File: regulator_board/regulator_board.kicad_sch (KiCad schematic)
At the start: 68 parts, among them J1 BATT, J10 5VOUT, J11 9VOUT, J12 9VOUT, J13 9VOUT, J2 5VOUT, J3 5VOUT, J4 5VOUT, J5 5VOUT, J6 5VOUT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

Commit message: regulator board title block
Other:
- company: (none) -> AUVCalStateLA
- title: (none) -> Regulator Board
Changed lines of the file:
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@@
 (kicad_sch (version 20211123) (generator eeschema)
   (paper "A4")
+  (title_block
+    (title "Regulator Board")
+    (date "2023-01-11")
+    (rev "dev1")
+    (company "AUVCalStateLA")
+  )
   (junction (at 160.02 86.36) (diameter 0) (color 0 0 0 0)
   )

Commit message: regulator component footprints
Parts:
- J1: footprint (none) -> Connector_AMASS:AMASS_XT60-M_1x02_P7.20mm_Vertical
- JP1, JP2, JP3, JP4: footprint (none) -> Jumper:SolderJumper-2_P1.3mm_Bridged_RoundedPad1.0x1.5mm
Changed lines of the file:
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@@
     (property "Reference" "JP3" (id 0) (at 166.37 80.01 0))
     (property "Value" "EN" (id 1) (at 166.37 82.55 0))
-    (property "Footprint" "" (id 2) (at 166.37 86.36 0)
+    (property "Footprint" "Jumper:SolderJumper-2_P1.3mm_Bridged_RoundedPad1.0x1.5mm" (id 2) (at 166.37 86.36 0)
       (effects (font (size 1.27 1.27)) hide)
     )
@@
     (property "Reference" "JP1" (id 0) (at 39.37 80.01 0))
     (property "Value" "EN" (id 1) (at 39.37 82.55 0))
-    (property "Footprint" "" (id 2) (at 39.37 86.36 0)
+    (property "Footprint" "Jumper:SolderJumper-2_P1.3mm_Bridged_RoundedPad1.0x1.5mm" (id 2) (at 39.37 86.36 0)
       (effects (font (size 1.27 1.27)) hide)
     )
@@
     (property "Reference" "JP4" (id 0) (at 166.37 130.81 0))
     (property "Value" "EN" (id 1) (at 166.37 133.35 0))
-    (property "Footprint" "" (id 2) (at 166.37 137.16 0)
+    (property "Footprint" "Jumper:SolderJumper-2_P1.3mm_Bridged_RoundedPad1.0x1.5mm" (id 2) (at 166.37 137.16 0)
       (effects (font (size 1.27 1.27)) hide)
     )
@@
     (property "Reference" "JP2" (id 0) (at 39.37 130.81 0))
     (property "Value" "EN" (id 1) (at 39.37 133.35 0))
-    (property "Footprint" "" (id 2) (at 39.37 137.16 0)
+    (property "Footprint" "Jumper:SolderJumper-2_P1.3mm_Bridged_RoundedPad1.0x1.5mm" (id 2) (at 39.37 137.16 0)
       (effects (font (size 1.27 1.27)) hide)
     )
@@
     (property "Reference" "J1" (id 0) (at 36.83 34.29 0))
     (property "Value" "BATT" (id 1) (at 36.83 36.83 0))
-    (property "Footprint" "" (id 2) (at 36.83 40.64 0)
+    (property "Footprint" "Connector_AMASS:AMASS_XT60-M_1x02_P7.20mm_Vertical" (id 2) (at 36.83 40.64 0)
       (effects (font (size 1.27 1.27)) hide)
     )
@@
     )
     (path "/b2e2fd19-798d-493c-9b57-86fa6fbcae53"
-      (reference "J1") (unit 1) (value "BATT") (footprint "")
+      (reference "J1") (unit 1) (value "BATT") (footprint "Connector_AMASS:AMASS_XT60-M_1x02_P7.20mm_Vertical")
     )
     (path "/580b5f68-7f84-4073-8ca8-221bc33e2978"
@@
     )
     (path "/2bf21a6a-e878-46f9-9e74-f711cf10453a"
-      (reference "JP1") (unit 1) (value "EN") (footprint "")
+      (reference "JP1") (unit 1) (value "EN") (footprint "Jumper:SolderJumper-2_P1.3mm_Bridged_RoundedPad1.0x1.5mm")
     )
     (path "/5a3ed22b-6215-4f1c-ae8e-2997d5637ba2"
-      (reference "JP2") (unit 1) (value "EN") (footprint "")
+      (reference "JP2") (unit 1) (value "EN") (footprint "Jumper:SolderJumper-2_P1.3mm_Bridged_RoundedPad1.0x1.5mm")
     )
     (path "/1ec1446c-1ce8-40a1-b2a2-29f00b72424b"
-      (reference "JP3") (unit 1) (value "EN") (footprint "")
+      (reference "JP3") (unit 1) (value "EN") (footprint "Jumper:SolderJumper-2_P1.3mm_Bridged_RoundedPad1.0x1.5mm")
     )
     (path "/4de0ee0c-c3e9-4dca-8da2-aaf3a6650e2e"
-      (reference "JP4") (unit 1) (value "EN") (footprint "")
+      (reference "JP4") (unit 1) (value "EN") (footprint "Jumper:SolderJumper-2_P1.3mm_Bridged_RoundedPad1.0x1.5mm")
     )
     (path "/318d6667-d175-4fcf-834c-669cc0534e5a"

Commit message: regulator board prelimiary completion
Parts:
- C1, C10, C11, C12, C13, C14, C15, C16, C17, C18, C19, C2, C20, C3, C4, C5, C6, C7, C8, C9: footprint (none) -> Capacitor_SMD:C_0603_1608Metric_Pad1.08x0.95mm_HandSolder
- D1, D2, D3, D4, D5: footprint (none) -> LED_SMD:LED_0603_1608Metric_Pad1.05x0.95mm_HandSolder
- F1: footprint (none) -> Fuse:Fuseholder_Blade_Mini_Keystone_3568
- F2, F3, F4, F5: footprint (none) -> Fuse:Fuse_0603_1608Metric_Pad1.05x0.95mm_HandSolder
- J10, J11, J12, J13, J2, J3, J4, J5, J6, J7, J8, J9: footprint (none) -> Connector_JST:JST_XH_B2B-XH-A_1x02_P2.50mm_Vertical
- L1, L2, L3, L4: footprint (none) -> AUVCSLA_FootLib:L_Bourns_SRP6030
- R1, R10, R11, R12, R13, R2, R3, R4, R5, R6, R7, R8, R9: footprint (none) -> Resistor_SMD:R_0603_1608Metric_Pad0.98x0.95mm_HandSolder
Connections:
- net 5V_2: now also C10.1, C8.1, C9.1, J5.1 (Pin_1), J6.1 (Pin_1), J7.1 (Pin_1), L2.2, R3.1; no longer C13.1, C14.1, C15.1, J10.1 (Pin_1), J8.1 (Pin_1), J9.1 (Pin_1), L3.2, R5.1
- net 5V_3: now also C13.1, C14.1, C15.1, J10.1 (Pin_1), J8.1 (Pin_1), J9.1 (Pin_1), L3.2, R5.1; no longer C10.1, C8.1, C9.1, J5.1 (Pin_1), J6.1 (Pin_1), J7.1 (Pin_1), L2.2, R3.1

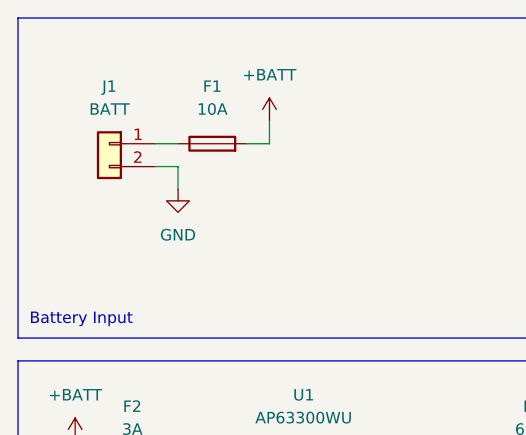
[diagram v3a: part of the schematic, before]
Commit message: fix regulator xt60 orientation
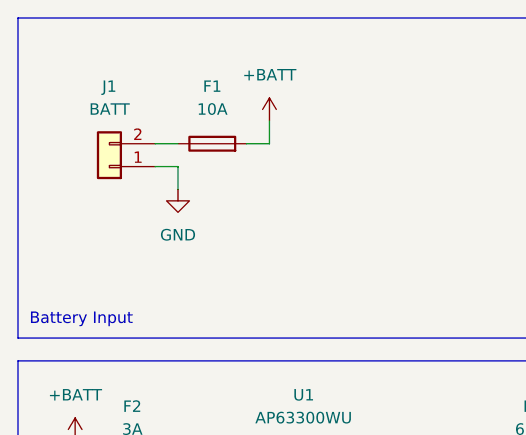
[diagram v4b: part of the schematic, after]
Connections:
- net GND: now also J1.1 (Pin_1); no longer J1.2 (Pin_2)
- net at F1.1: now also J1.2 (Pin_2); no longer J1.1 (Pin_1)
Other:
- moved on the sheet: J1
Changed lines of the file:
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@@
     (pin "2")
   )
-  (symbol (lib_id "Connector_Generic:Conn_01x02") (at 36.83 40.64 0) (mirror y) (unit 1)
+  (symbol (lib_id "Connector_Generic:Conn_01x02") (at 36.83 43.18 180) (unit 1)
     (in_bom yes) (on_board yes) (fields_autoplaced)
     (property "Reference" "J1" (id 0) (at 36.83 34.29 0))
     (property "Value" "BATT" (id 1) (at 36.83 36.83 0))
-    (property "Footprint" "Connector_AMASS:AMASS_XT60-M_1x02_P7.20mm_Vertical" (id 2) (at 36.83 40.64 0)
+    (property "Footprint" "Connector_AMASS:AMASS_XT60-M_1x02_P7.20mm_Vertical" (id 2) (at 36.83 43.18 0)
       (effects (font (size 1.27 1.27)) hide)
     )
-    (property "Datasheet" "~" (id 3) (at 36.83 40.64 0)
+    (property "Datasheet" "~" (id 3) (at 36.83 43.18 0)
       (effects (font (size 1.27 1.27)) hide)
     )

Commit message: regulator board outline redesign & back graphics
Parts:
- added H1, H2, H3, H4: MountingHole_Pad, MountingHole:MountingHole_3.2mm_M3_Pad_Via, symbol Mechanical:MountingHole_Pad
- added LOGO1: Logo_Open_Hardware_Large, Symbol:OSHW-Logo2_9.8x8mm_SilkScreen, symbol Graphic:Logo_Open_Hardware_Large
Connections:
- net GND: now also H1.1, H2.1, H3.1, H4.1
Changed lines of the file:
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@@
   (junction (at 237.49 146.05) (diameter 0) (color 0 0 0 0)
   )
+  (junction (at 92.71 175.26) (diameter 0) (color 0 0 0 0)
+  )
   (junction (at 99.06 76.2) (diameter 0) (color 0 0 0 0)
   )
@@
   (junction (at 77.47 127) (diameter 0) (color 0 0 0 0)
   )
+  (junction (at 92.71 180.34) (diameter 0) (color 0 0 0 0)
+  )
   (junction (at 130.81 83.82) (diameter 0) (color 0 0 0 0)
   )
@@
   (junction (at 237.49 133.35) (diameter 0) (color 0 0 0 0)
   )
+  (junction (at 92.71 185.42) (diameter 0) (color 0 0 0 0)
+  )
   (junction (at 257.81 134.62) (diameter 0) (color 0 0 0 0)
   )
@@
     (stroke (width 0) (type default) (color 0 0 0 0))
   )
+  (wire (pts (xy 92.71 180.34) (xy 92.71 185.42))
+    (stroke (width 0) (type default) (color 0 0 0 0))
+  )
   (wire (pts (xy 226.06 137.16) (xy 226.06 139.7))
     (stroke (width 0) (type default) (color 0 0 0 0))
@@
     (stroke (width 0) (type default) (color 0 0 0 0))
   )
+  (wire (pts (xy 92.71 170.18) (xy 92.71 175.26))
+    (stroke (width 0) (type default) (color 0 0 0 0))
+  )
   (wire (pts (xy 73.66 78.74) (xy 73.66 86.36))
     (stroke (width 0) (type default) (color 0 0 0 0))
@@
     (stroke (width 0) (type default) (color 0 0 0 0))
   )
+  (wire (pts (xy 90.17 175.26) (xy 92.71 175.26))
+    (stroke (width 0) (type default) (color 0 0 0 0))
+  )
   (wire (pts (xy 77.47 76.2) (xy 77.47 78.74))
     (stroke (width 0) (type default) (color 0 0 0 0))
@@
     (stroke (width 0) (type default) (color 0 0 0 0))
   )
+  (wire (pts (xy 90.17 185.42) (xy 92.71 185.42))
+    (stroke (width 0) (type default) (color 0 0 0 0))
+  )
   (wire (pts (xy 110.49 127) (xy 130.81 127))
     (stroke (width 0) (type default) (color 0 0 0 0))
@@
     (stroke (width 0) (type default) (color 0 0 0 0))
   )
+  (wire (pts (xy 92.71 185.42) (xy 92.71 187.96))
+    (stroke (width 0) (type default) (color 0 0 0 0))
+  )
   (polyline (pts (xy 151.13 115.57) (xy 151.13 163.83))
     (stroke (width 0) (type default) (color 0 0 0 0))
@@
     (stroke (width 0) (type default) (color 0 0 0 0))
   )
+  (wire (pts (xy 90.17 180.34) (xy 92.71 180.34))
+    (stroke (width 0) (type default) (color 0 0 0 0))
+  )
   (polyline (pts (xy 26.67 62.23) (xy 151.13 62.23))
     (stroke (width 0) (type default) (color 0 0 0 0))
@@
     (stroke (width 0) (type default) (color 0 0 0 0))
   )
+  (wire (pts (xy 92.71 175.26) (xy 92.71 180.34))
+    (stroke (width 0) (type default) (color 0 0 0 0))
+  )
   (wire (pts (xy 135.89 134.62) (xy 130.81 134.62))
+    (stroke (width 0) (type default) (color 0 0 0 0))
+  )
+  (wire (pts (xy 92.71 170.18) (xy 90.17 170.18))
     (stroke (width 0) (type default) (color 0 0 0 0))
   )
@@
   (label "5V_2" (at 111.76 127 0)
     (effects (font (size 1.27 1.27)) (justify left bottom))
+  )
+  (symbol (lib_id "Mechanical:MountingHole_Pad") (at 87.63 175.26 90) (unit 1)
+    (in_bom yes) (on_board yes)
+    (property "Reference" "H2" (id 0) (at 80.01 173.99 90))
+    (property "Value" "MountingHole_Pad" (id 1) (at 73.66 176.53 90))
+    (property "Footprint" "MountingHole:MountingHole_3.2mm_M3_Pad_Via" (id 2) (at 87.63 175.26 0)
+      (effects (font (size 1.27 1.27)) hide)
+    )
+    (property "Datasheet" "~" (id 3) (at 87.63 175.26 0)
+      (effects (font (size 1.27 1.27)) hide)
+    )
+    (pin "1")
+  )
+  (symbol (lib_id "Mechanical:MountingHole_Pad") (at 87.63 180.34 90) (unit 1)
+    (in_bom yes) (on_board yes)
+    (property "Reference" "H3" (id 0) (at 80.01 179.07 90))
+    (property "Value" "MountingHole_Pad" (id 1) (at 73.66 181.61 90))
+    (property "Footprint" "MountingHole:MountingHole_3.2mm_M3_Pad_Via" (id 2) (at 87.63 180.34 0)
+      (effects (font (size 1.27 1.27)) hide)
+    )
+    (property "Datasheet" "~" (id 3) (at 87.63 180.34 0)
+      (effects (font (size 1.27 1.27)) hide)
+    )
+    (pin "1")
   )
   (symbol (lib_id "Connector_Generic:Conn_01x02") (at 140.97 142.24 0) (unit 1)
@@
     (pin "2")
   )
+  (symbol (lib_id "Mechanical:MountingHole_Pad") (at 87.63 170.18 90) (unit 1)
+    (in_bom yes) (on_board yes)
+    (property "Reference" "H1" (id 0) (at 80.01 168.91 90))
+    (property "Value" "MountingHole_Pad" (id 1) (at 73.66 171.45 90))
+    (property "Footprint" "MountingHole:MountingHole_3.2mm_M3_Pad_Via" (id 2) (at 87.63 170.18 0)
+      (effects (font (size 1.27 1.27)) hide)
+    )
+    (property "Datasheet" "~" (id 3) (at 87.63 170.18 0)
+      (effects (font (size 1.27 1.27)) hide)
+    )
+    (pin "1")
+  )
   (symbol (lib_id "Device:C") (at 248.92 139.7 0) (unit 1)
     (in_bom yes) (on_board yes) (fields_autoplaced)
@@
     (pin "2")
   )
+  (symbol (lib_id "power:GND") (at 92.71 187.96 0) (unit 1)
+    (in_bom yes) (on_board yes) (fields_autoplaced)
+    (property "Reference" "#PWR0101" (id 0) (at 92.71 194.31 0)
+      (effects (font (size 1.27 1.27)) hide)
+    )
+    (property "Value" "GND" (id 1) (at 92.71 193.04 0))
+    (property "Footprint" "" (id 2) (at 92.71 187.96 0)
+      (effects (font (size 1.27 1.27)) hide)
+    )
+    (property "Datasheet" "" (id 3) (at 92.71 187.96 0)
+      (effects (font (size 1.27 1.27)) hide)
+    )
+    (pin "1")
+  )
   (symbol (lib_id "power:+BATT") (at 160.02 73.66 0) (unit 1)
     (in_bom yes) (on_board yes) (fields_autoplaced)
@@
     (pin "1")
     (pin "2")
+  )
+  (symbol (lib_id "Mechanical:MountingHole_Pad") (at 87.63 185.42 90) (unit 1)
+    (in_bom yes) (on_board yes)
+    (property "Reference" "H4" (id 0) (at 80.01 184.15 90))
+    (property "Value" "MountingHole_Pad" (id 1) (at 73.66 186.69 90))
+    (property "Footprint" "MountingHole:MountingHole_3.2mm_M3_Pad_Via" (id 2) (at 87.63 185.42 0)
+      (effects (font (size 1.27 1.27)) hide)
+    )
+    (property "Datasheet" "~" (id 3) (at 87.63 185.42 0)
+      (effects (font (size 1.27 1.27)) hide)
+    )
+    (pin "1")
   )
   (symbol (lib_id "power:+BATT") (at 160.02 124.46 0) (unit 1)
@@
     (pin "1")
   )
+  (symbol (lib_id "Graphic:Logo_Open_Hardware_Large") (at 25.4 186.69 0) (unit 1)
+    (in_bom yes) (on_board yes) (fields_autoplaced)
+    (property "Reference" "LOGO1" (id 0) (at 25.4 173.99 0)
+      (effects (font (size 1.27 1.27)) hide)
+    )
+    (property "Value" "Logo_Open_Hardware_Large" (id 1) (at 25.4 196.85 0)
+      (effects (font (size 1.27 1.27)) hide)
+    )
+    (property "Footprint" "Symbol:OSHW-Logo2_9.8x8mm_SilkScreen" (id 2) (at 25.4 186.69 0)
+      (effects (font (size 1.27 1.27)) hide)
+    )
+    (property "Datasheet" "~" (id 3) (at 25.4 186.69 0)
+      (effects (font (size 1.27 1.27)) hide)
+    )
+  )
   (symbol (lib_id "AUVCSLA_SymbLib:AP63300WU") (at 58.42 129.54 0) (unit 1)
     (in_bom yes) (on_board yes) (fields_autoplaced)
@@
       (reference "#PWR016") (unit 1) (value "GND") (footprint "")
     )
+    (path "/869dc4b5-e754-4b8c-848e-4dcdd715e201"
+      (reference "#PWR0101") (unit 1) (value "GND") (footprint "")
+    )
     (path "/59083358-b07e-45cb-a727-049ad4aafa79"
       (reference "C1") (unit 1) (value "10u") (footprint "Capacitor_SMD:C_0603_1608Metric_Pad1.08x0.95mm_HandSolder")
@@
       (reference "F5") (unit 1) (value "3A") (footprint "Fuse:Fuse_0603_1608Metric_Pad1.05x0.95mm_HandSolder")
     )
+    (path "/60cba3a3-7cac-42a8-86cf-d28664ab2bd2"
+      (reference "H1") (unit 1) (value "MountingHole_Pad") (footprint "MountingHole:MountingHole_3.2mm_M3_Pad_Via")
+    )
+    (path "/047656ac-d791-43eb-94bd-5b6b9ee28766"
+      (reference "H2") (unit 1) (value "MountingHole_Pad") (footprint "MountingHole:MountingHole_3.2mm_M3_Pad_Via")
+    )
+    (path "/050c3c15-ca97-4178-840c-343385b57487"
+      (reference "H3") (unit 1) (value "MountingHole_Pad") (footprint "MountingHole:MountingHole_3.2mm_M3_Pad_Via")
+    )
+    (path "/9bc0e347-a1bf-4c93-95a6-551f3d95f12c"
+      (reference "H4") (unit 1) (value "MountingHole_Pad") (footprint "MountingHole:MountingHole_3.2mm_M3_Pad_Via")
+    )
     (path "/b2e2fd19-798d-493c-9b57-86fa6fbcae53"
       (reference "J1") (unit 1) (value "BATT") (footprint "Connector_AMASS:AMASS_XT60-M_1x02_P7.20mm_Vertical")
@@
       (reference "L4") (unit 1) (value "10u") (footprint "AUVCSLA_FootLib:L_Bourns_SRP6030")
     )
+    (path "/be057cc2-499f-499d-ab7c-e5f89e997d45"
+      (reference "LOGO1") (unit 1) (value "Logo_Open_Hardware_Large") (footprint "Symbol:OSHW-Logo2_9.8x8mm_SilkScreen")
+    )
     (path "/d891538d-fc0c-4a84-aaa4-4635670b1000"
